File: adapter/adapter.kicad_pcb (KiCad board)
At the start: 2 copper layers, 96 x 18 mm, 24 parts, among them J1 MALE, J11 MALE, J12 FEMALE, J13 STANDOFF, J14 STANDOFF, J15 STANDOFF, J2 FEMALE, J3 STANDOFF, J4 STANDOFF, J5 STANDOFF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

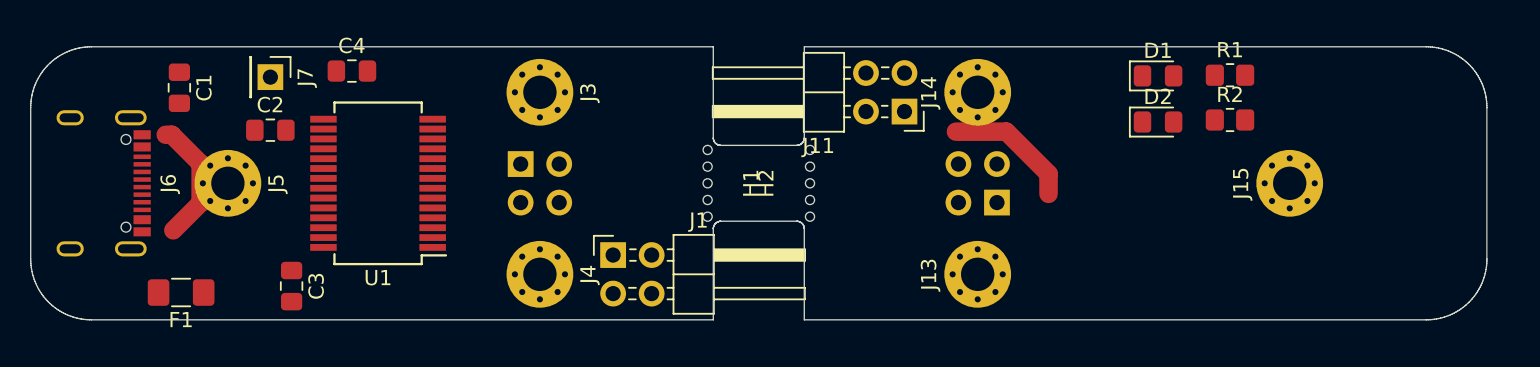
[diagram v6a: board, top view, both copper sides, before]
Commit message: Route top board
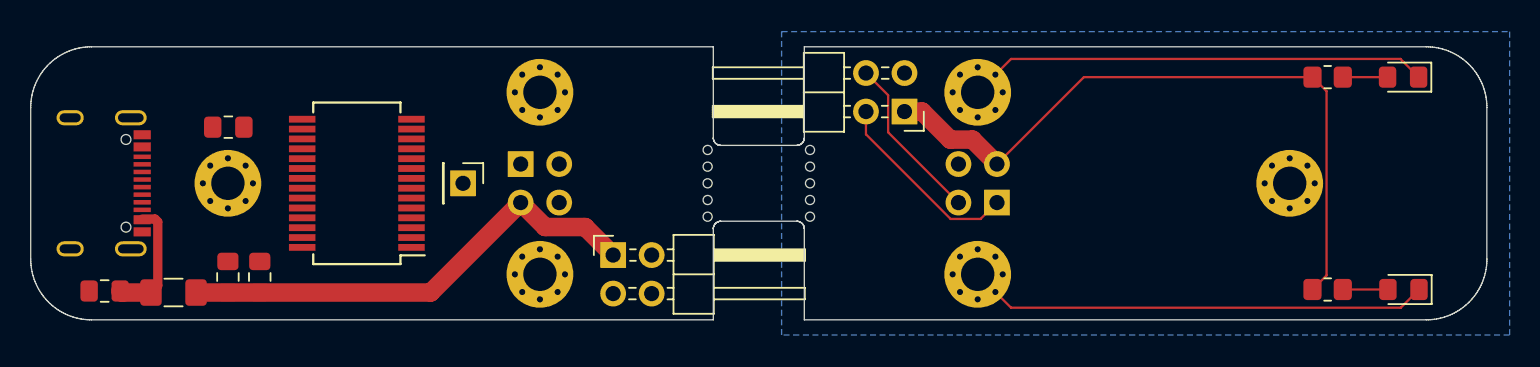
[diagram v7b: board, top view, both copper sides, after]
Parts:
- moved D1 21.4 mm to (191.0, 112.0), turned to 180 degrees
- moved D2 16.4 mm to (191.0, 98.0), turned to 180 degrees
- moved R1 15.5 mm to (186.0, 112.0)
- moved C4 14.9 mm to (115.6, 111.2), turned to 90 degrees
- moved J7 14.5 mm to (129.0, 105.0)
- moved C1 14.3 mm to (105.4, 112.1), turned to 0 degrees
- moved R2 7.03 mm to (186.0, 98.0)
- moved C3 4.24 mm to (113.5, 111.2)
- moved C2 2.78 mm to (113.5, 101.3), turned to 180 degrees
- moved U1 1.40 mm to (122.0, 105.0)
- moved F1 0.50 mm to (109.9, 112.2)
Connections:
- C1 pad 1: GND -> GNDB
- C2 pad 2: GND -> GNDB
- C3 pad 1: GND -> GNDB
- C3 pad 2: +5V -> +5VB
- C4 pad 1: +5V -> +5VB
- C4 pad 2: GND -> GNDB
- F1 pad 1: +5V -> +5VB
- J1 pad 1: +5V -> +5VB
- J1 pad 3: GND -> GNDB
- J2 pad 3: +5V -> +5VB
- J2 pad 4: GND -> GNDB
- J6 pad A1: GND -> GNDB
- J6 pad A12: GND -> GNDB
- J6 pad B1: GND -> GNDB
- J6 pad B12: GND -> GNDB
- J6 pad S1: GND -> GNDB
- U1 pad 18: GND -> GNDB
- U1 pad 20: +5V -> +5VB
- U1 pad 21: GND -> GNDB
- U1 pad 25: GND -> GNDB
- U1 pad 26: GND -> GNDB
- U1 pad 4: +5V -> +5VB
- U1 pad 7: GND -> GNDB
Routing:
- net +5V: track 0.00 -> 45.5 mm
- net +5VB: track 0.00 -> 31.4 mm
- net Net-(D1-Pad1): track 0.00 -> 30.5 mm
- net Net-(D2-Pad1): track 0.00 -> 30.5 mm
- net Net-(J11-Pad2): track 0.00 -> 12.9 mm
- net Net-(J11-Pad4): track 0.00 -> 11.1 mm
- net (no net): track 8.58 -> 0.00 mm
- net Net-(J5-Pad1): track 8.23 -> 0.00 mm
- net /Lower Board/VBUS: track 0.00 -> 8.02 mm
- net Net-(D1-Pad2): track 0.00 -> 2.97 mm
- net Net-(D2-Pad2): track 0.00 -> 2.95 mm
- added copper zone on B.Cu, net GND

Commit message: Finish routing
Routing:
- net /Lower Board/TXD: track 0.00 -> 24.1 mm
- net /Lower Board/RXD: track 0.00 -> 22.4 mm
- net /Lower Board/D+: track 0.00 -> 20.5 mm
- net /Lower Board/RXLED: track 0.00 -> 19.3 mm, vias 0 -> 1
- net /Lower Board/TXLED: track 0.00 -> 18.9 mm
- net /Lower Board/D-: track 0.00 -> 17.1 mm, vias 0 -> 2
- net +5VB: track 31.4 -> 46.8 mm
- net GNDB: track 0.00 -> 10.2 mm, vias 0 -> 5
- net /Lower Board/VBUS: track 8.02 -> 16.8 mm
- net /Lower Board/DTR: track 0.00 -> 5.59 mm
- net Net-(C2-Pad1): track 0.00 -> 4.17 mm
- added copper zone on F.Cu, net GND
- added copper zone on B.Cu, net GNDB
- added copper zone on F.Cu, net GNDB
